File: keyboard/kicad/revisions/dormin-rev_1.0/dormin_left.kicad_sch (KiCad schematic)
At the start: 103 parts, among them J2 Conn_01x04, Q1 AO3400A, Q2 AO3407A, SW1 SW_Push, SW10 SW_Push, SW11 SW_Push, SW12 SW_Push, SW13 SW_Push, SW14 SW_Push, SW15 SW_Push, SW16 SW_Push, SW17 SW_Push, SW18 SW_Push, SW19 SW_Push, SW2 SW_Push, SW20 SW_Push, SW3 SW_Push, SW4 SW_Push, SW5 SW_Push, SW6 SW_Push, SW7 SW_Push, SW8 SW_Push, SW9 SW_Push, U3 XIAO-nRF52840-SMD

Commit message: feat: added footprints | partial
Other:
- note removed: "D O R M I N"
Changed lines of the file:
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@@
-		)
-	)
-	(text "D O R M I N"
-		(exclude_from_sim no)
-		(at 25.654 235.458 0)
-		(effects
-			(font
-				(face "KiCad Font")
-				(size 14.732 14.732)
-			)
-			(justify left bottom)
 		)
 	)

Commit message: chore: added temporary routing
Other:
- note added: "D O R M I N"
- moved on the sheet: J2, TP1, TP3, U3

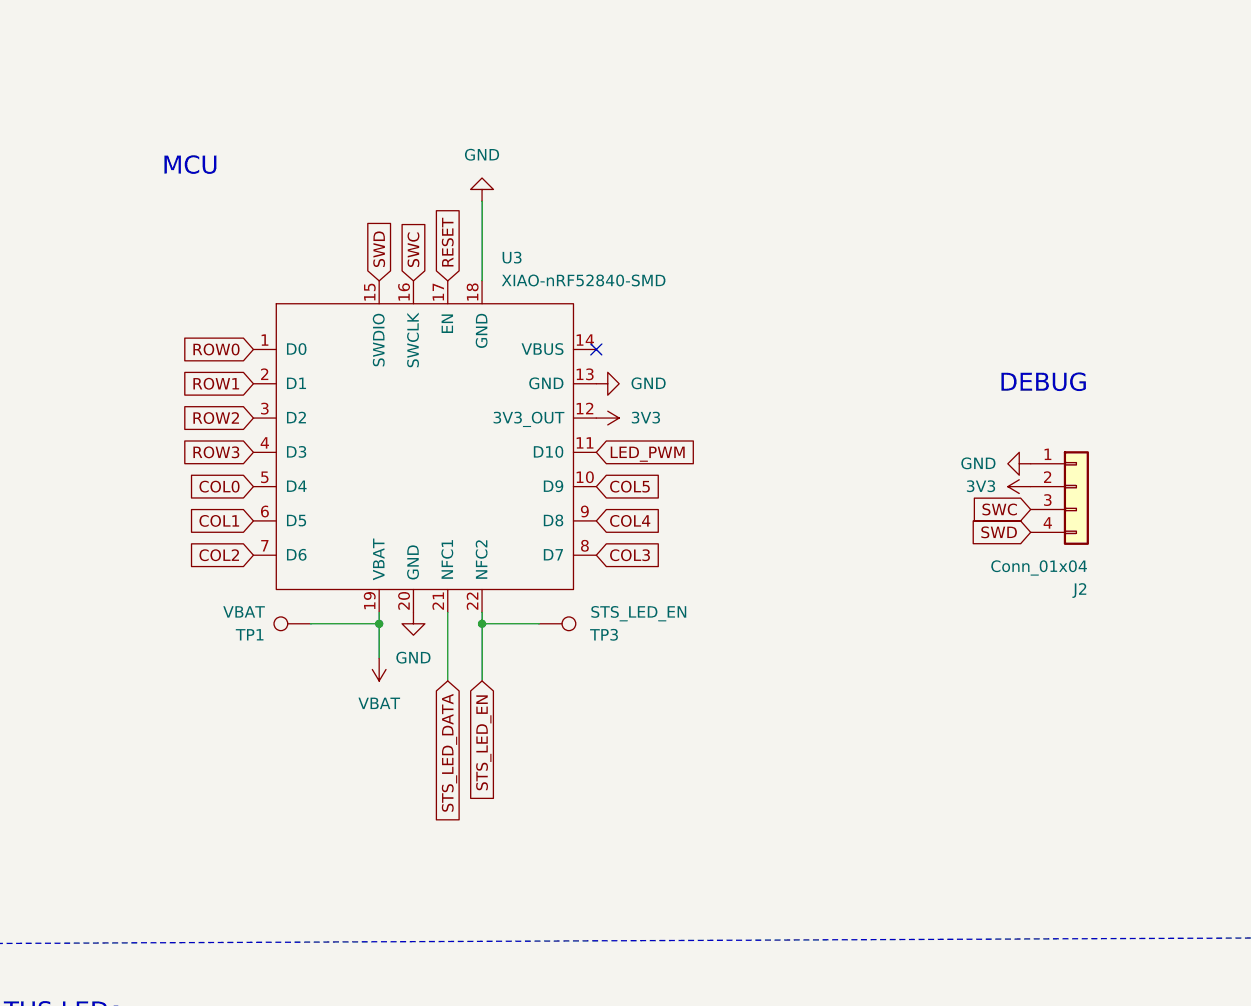
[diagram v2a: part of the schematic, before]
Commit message: chore: finish main routing
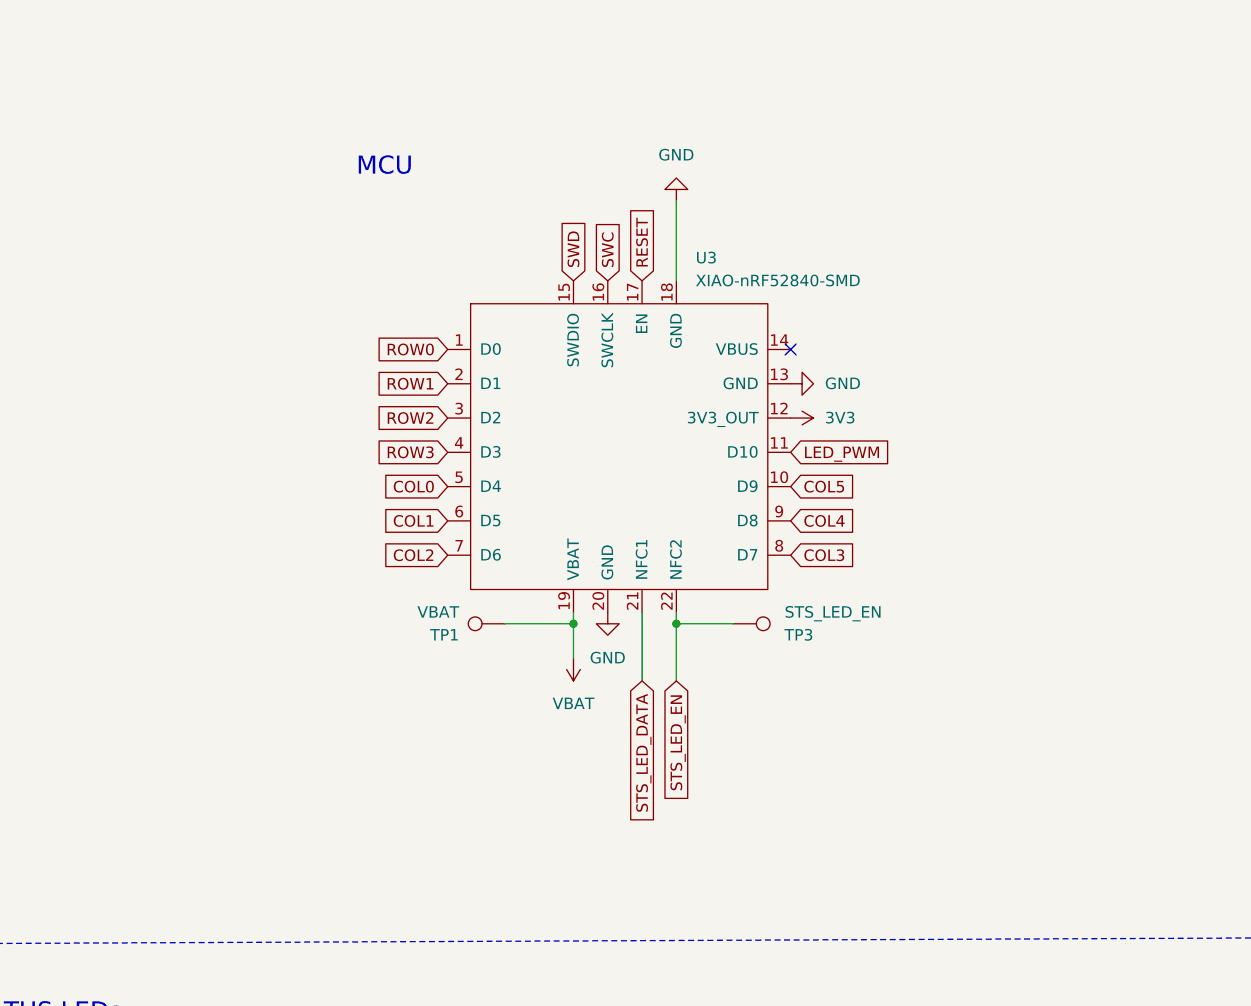
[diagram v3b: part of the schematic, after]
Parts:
- removed J2: Conn_01x04, Connector_PinSocket_2.54mm:PinSocket_1x04_P2.54mm_Vertical, symbol Connector_Generic:Conn_01x04
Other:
- note removed: "DEBUG"
- moved on the sheet: TP1, TP3, U3
